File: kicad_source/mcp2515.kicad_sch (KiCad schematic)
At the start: 15 parts, among them CN4 SM04B-GHS-TB, CN5 SM04B-GHS-TB, U8 MCP2515T-I/SO, U9 SN65HVD230, Y1 X322516MLB4SI

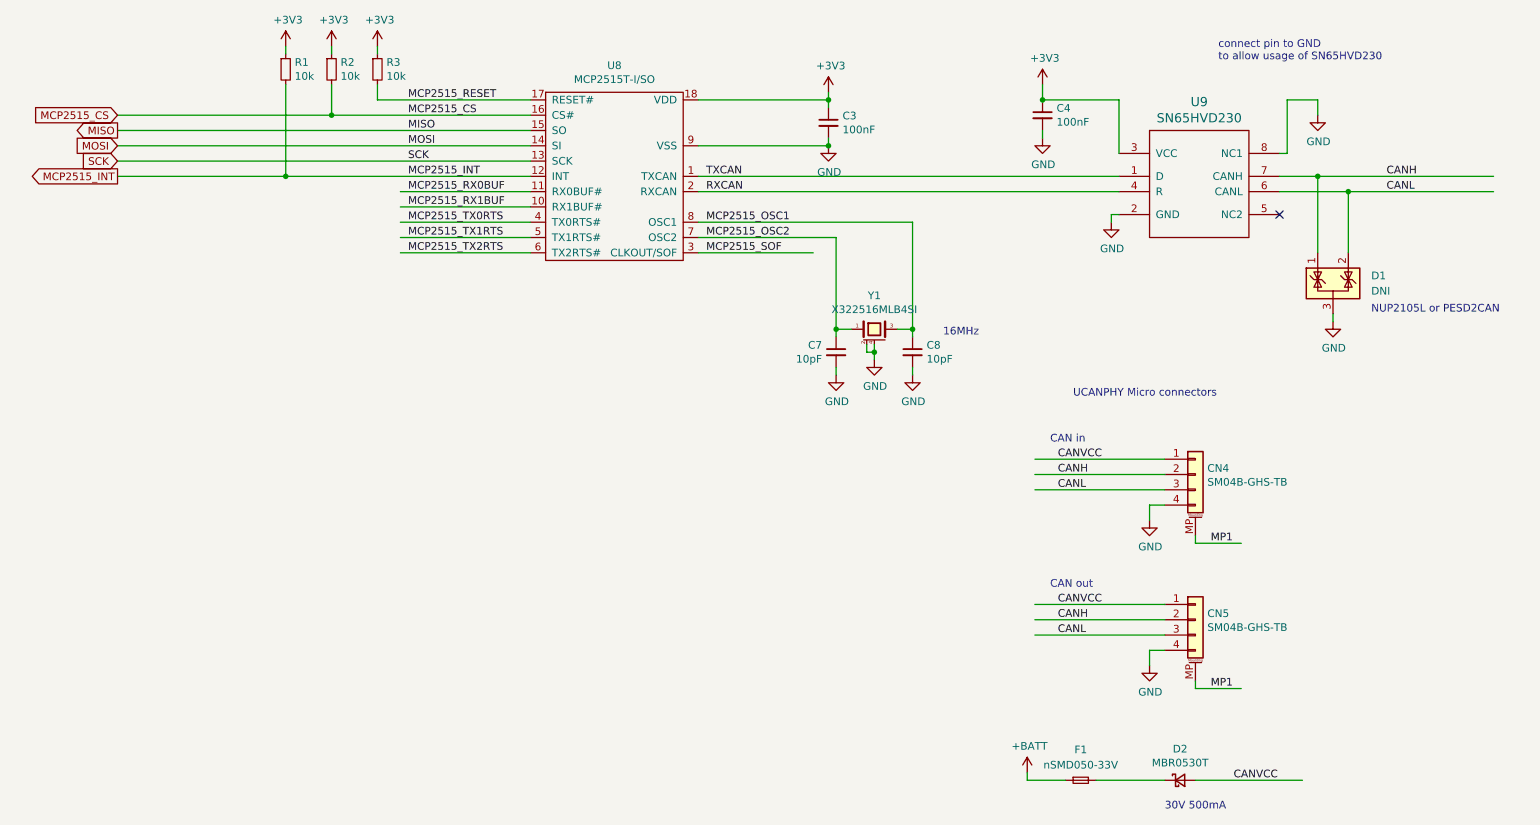
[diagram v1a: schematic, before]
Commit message: added GNSS u-blox max-m10
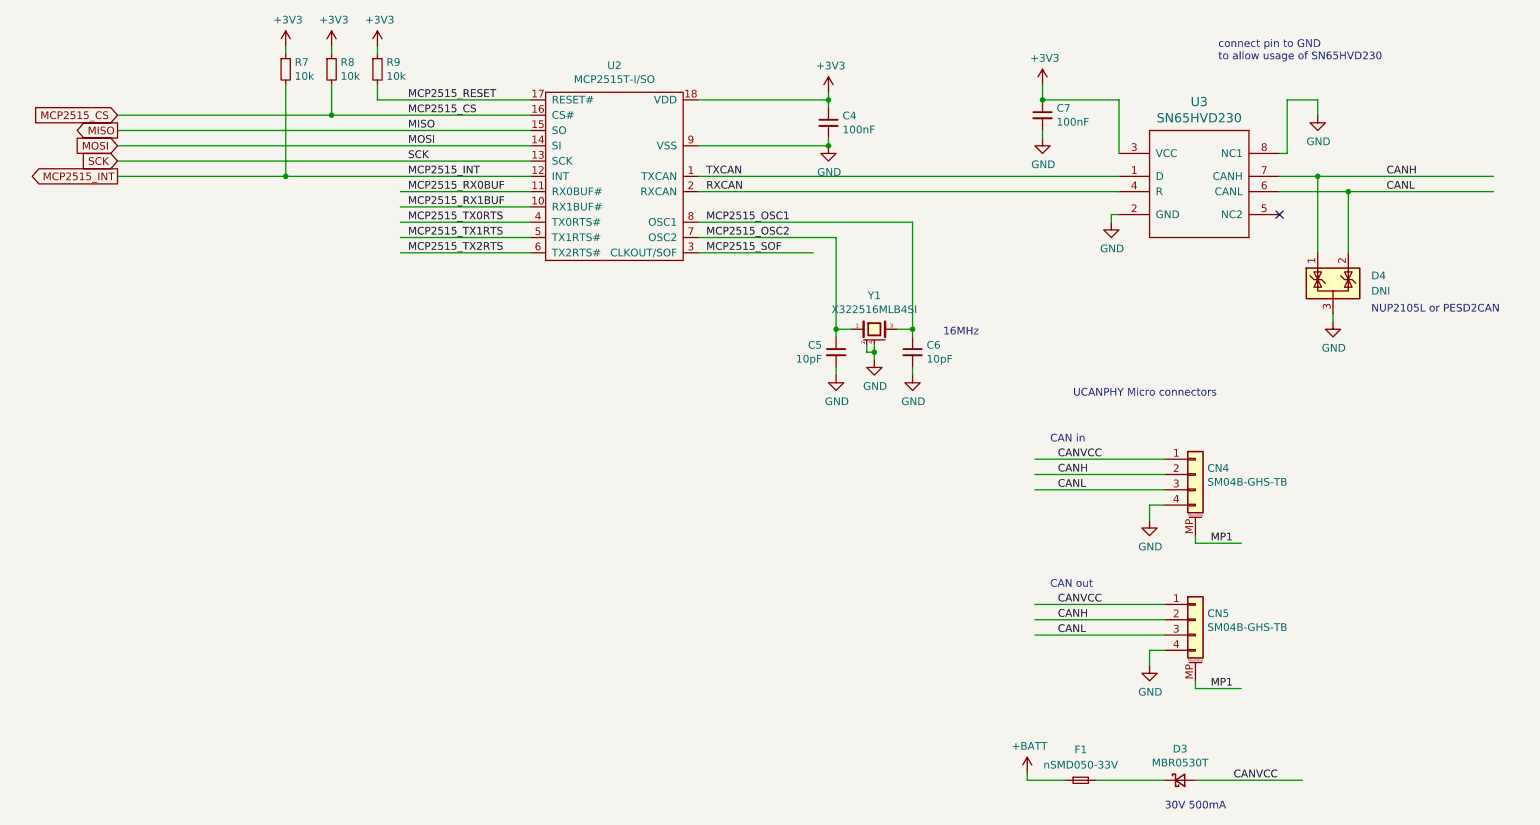
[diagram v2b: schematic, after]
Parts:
- renumbered C3 to C4, C7 to C5, C8 to C6, C4 to C7, D2 to D3, D1 to D4, R1 to R7, R2 to R8, R3 to R9, U8 to U2, U9 to U3
